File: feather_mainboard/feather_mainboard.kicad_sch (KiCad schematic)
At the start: 4 parts

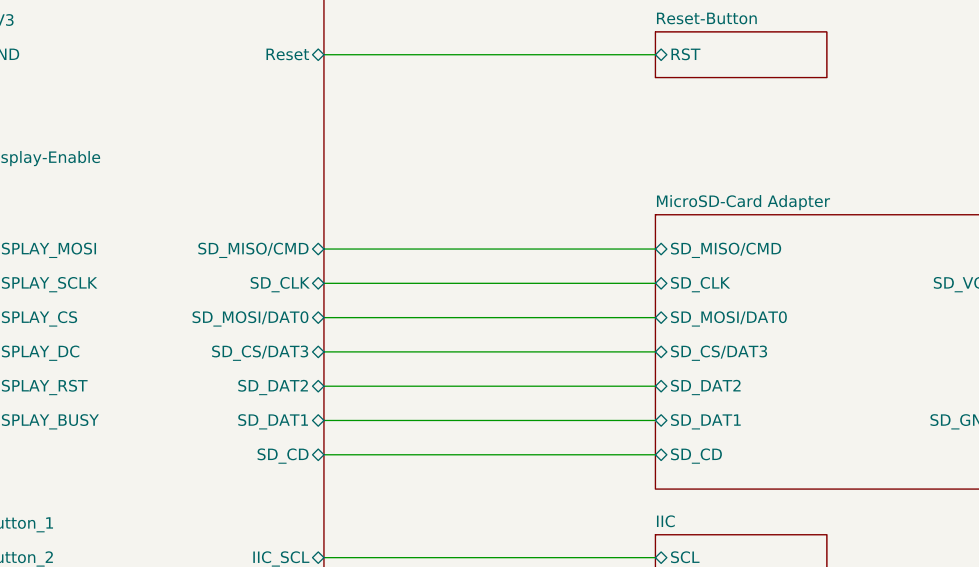
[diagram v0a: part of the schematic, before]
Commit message: Corrected/switched the names of MISO and MOSI pins
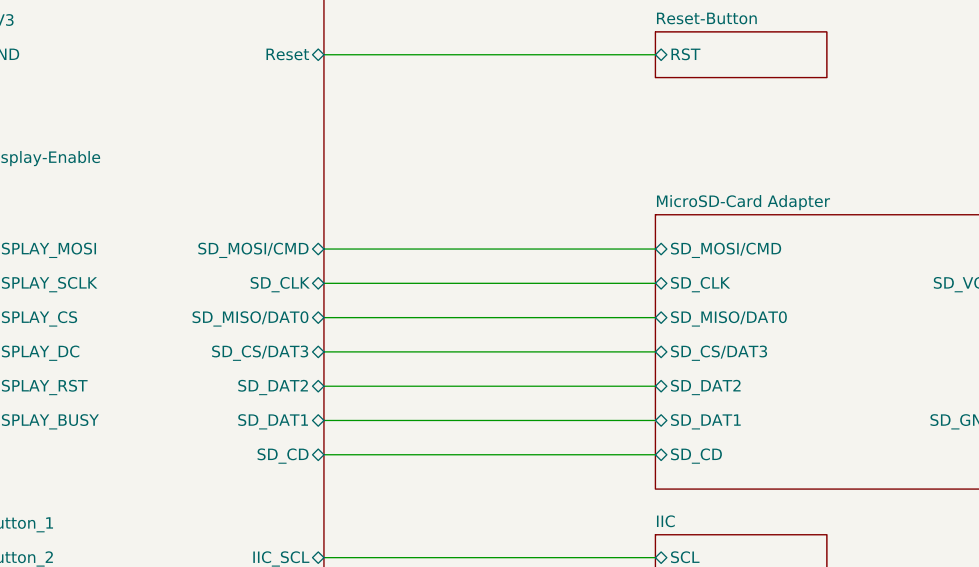
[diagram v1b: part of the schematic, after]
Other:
- sheet MicroSD-Card Adapter ports: added SD_MISO/DAT0, SD_MOSI/CMD; removed SD_MISO/CMD, SD_MOSI/DAT0
- sheet Microcontroller ports: added SD_MISO/DAT0, SD_MOSI/CMD; removed SD_MISO/CMD, SD_MOSI/DAT0
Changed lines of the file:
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@@
-			)
-		)
-		(pin "SD_MOSI{slash}DAT0" bidirectional
-			(at 172.72 92.71 0)
-			(effects
-				(font
-					(size 1.27 1.27)
-				)
-				(justify right)
 			)
 		)
 		(pin "SD_CLK" bidirectional
 			(at 172.72 88.9 0)
-			(effects
-				(font
-					(size 1.27 1.27)
-				)
-				(justify right)
-			)
-		)
-		(pin "SD_MISO{slash}CMD" bidirectional
-			(at 172.72 85.09 0)
 			(effects
 				(font
@@
 				)
 				(justify left)
+			)
+		)
+		(pin "SD_MOSI{slash}CMD" bidirectional
+			(at 172.72 85.09 0)
+			(effects
+				(font
+					(size 1.27 1.27)
+				)
+				(justify right)
+			)
+		)
+		(pin "SD_MISO{slash}DAT0" bidirectional
+			(at 172.72 92.71 0)
+			(effects
+				(font
+					(size 1.27 1.27)
+				)
+				(justify right)
 			)
 		)
@@
 			)
 		)
-		(pin "SD_MISO{slash}CMD" bidirectional
-			(at 209.55 85.09 180)
-			(effects
-				(font
-					(size 1.27 1.27)
-				)
-				(justify left)
-			)
-		)
 		(pin "SD_DAT1" bidirectional
 			(at 209.55 104.14 180)
@@
 				)
 				(justify right)
-			)
-		)
-		(pin "SD_MOSI{slash}DAT0" bidirectional
-			(at 209.55 92.71 180)
-			(effects
-				(font
-					(size 1.27 1.27)
-				)
-				(justify left)
 			)
 		)
@@
 			(effects
 				(font
+					(size 1.27 1.27)
+				)
+				(justify left)
+			)
+		)
+		(pin "SD_MOSI{slash}CMD" bidirectional
+			(at 209.55 85.09 180)
+			(effects
+				(font
+					(size 1.27 1.27)
+				)
+				(justify left)
+			)
+		)
+		(pin "SD_MISO{slash}DAT0" bidirectional
+			(at 209.55 92.71 180)
+			(effects
+				(font

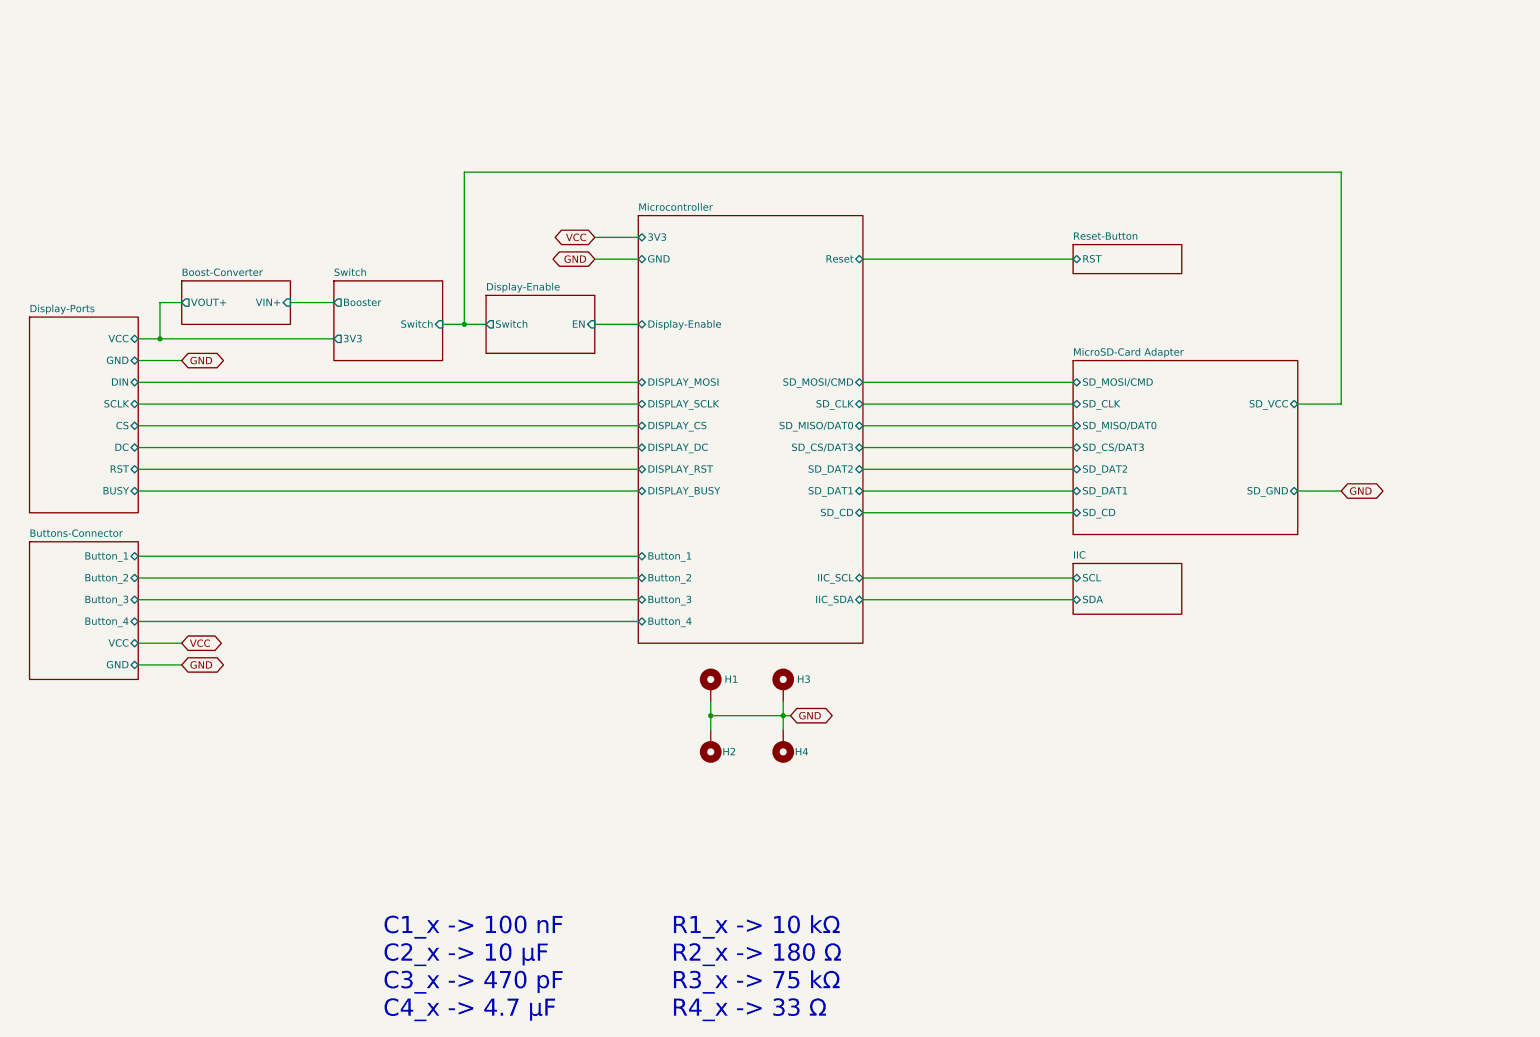
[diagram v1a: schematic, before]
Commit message: Updated the mainboard: removed unnecessary pull-ups on SD card lines; connected IIC pull-ups to enable circuit; cleaned up schematic
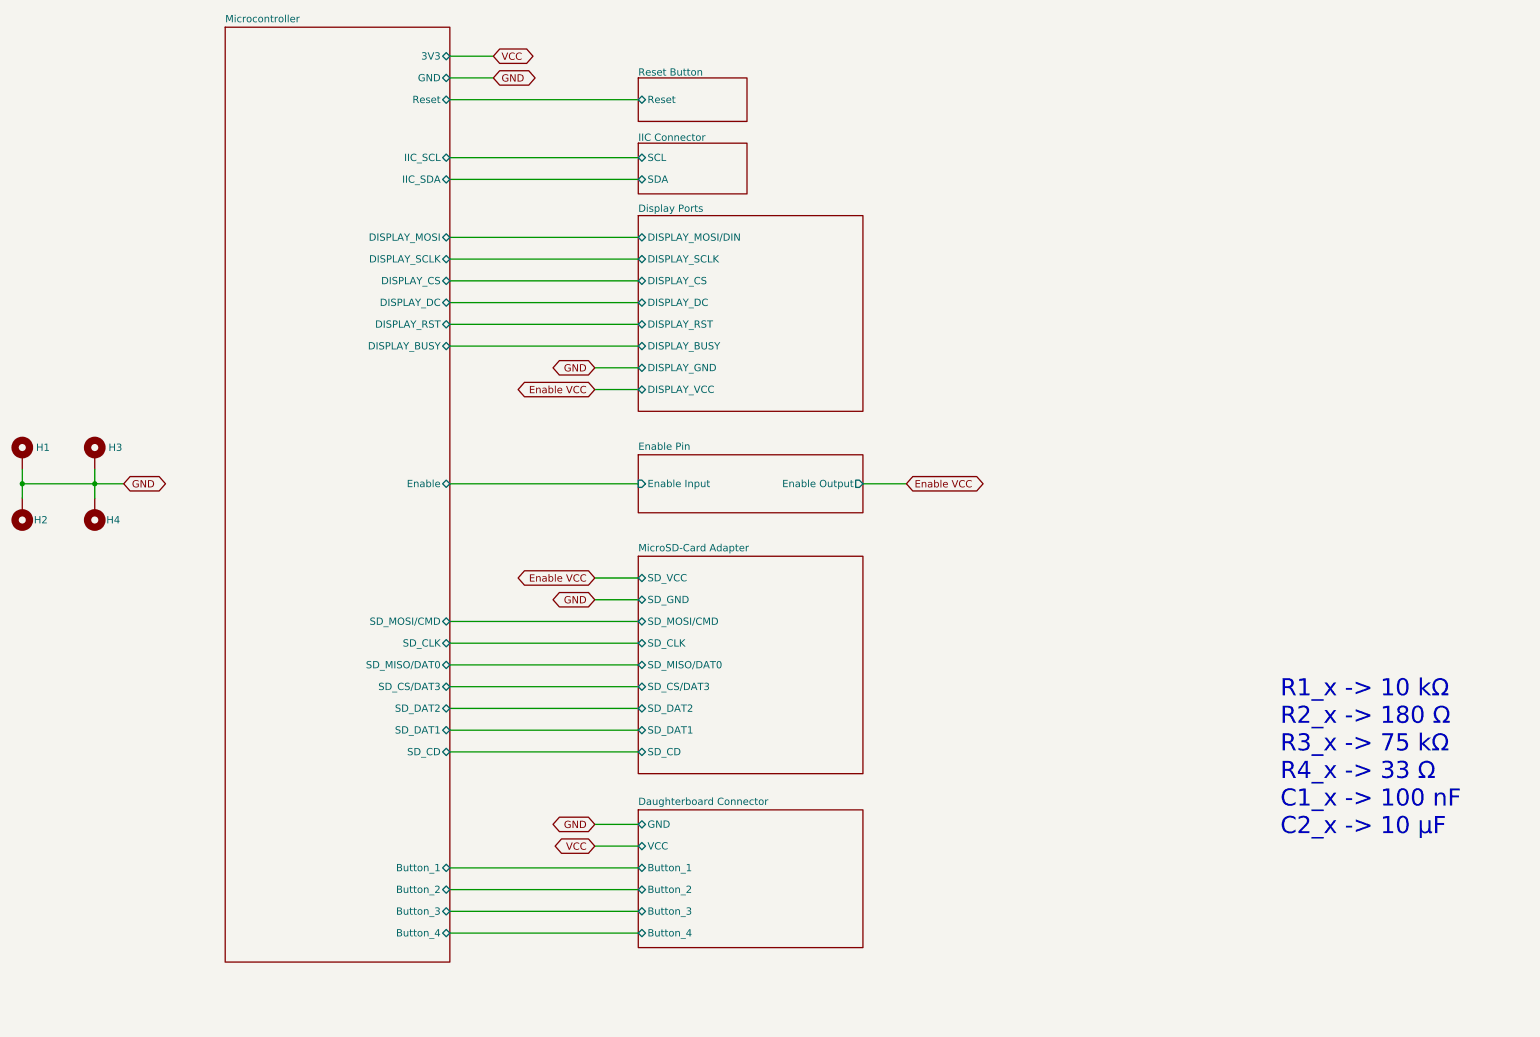
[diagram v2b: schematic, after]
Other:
- removed sheet Boost-Converter
- removed sheet Buttons-Connector
- removed sheet Display-Enable
- removed sheet Display-Ports
- removed sheet IIC
- removed sheet Reset-Button
- removed sheet Switch
- added sheet Daughterboard Connector (buttons-connector.kicad_sch)
- added sheet Display Ports (display_ports.kicad_sch)
- added sheet Enable Pin (display_enable.kicad_sch)
- added sheet IIC Connector (iic.kicad_sch)
- added sheet Reset Button (reset-button.kicad_sch)
- sheet Microcontroller ports: added Enable; removed Display-Enable
- note added: "R1_x -> 10 kΩ R2_x -> 180 Ω R3_x -> 75 kΩ R4_x -> 33 Ω C1_x -> 100 nF C2_x -> 10 µF"
- note removed: "C1_x -> 100 nF C2_x -> 10 µF C3_x -> 470 pF C4_x -> 4.7 µF"
- note removed: "R1_x -> 10 kΩ R2_x -> 180 Ω R3_x -> 75 kΩ R4_x -> 33 Ω"
- company: Benjamin Klaric -> Benjamin Klarić
- moved on the sheet: H1, H2, H3, H4
